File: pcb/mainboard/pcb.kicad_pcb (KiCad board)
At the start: 4 copper layers, 67.2 x 58.2 mm, 225 parts, among them J401 AudioJack3, J501 Conn_02x15_Odd_Even_MountingP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, J601 Conn_01x40_MountingPin, J801 USB_B_Mini, J901 U.FL Connector, SW101 SW_Push, SW201 SW_Push, U101 PCA9450BHN, U102 BQ27441-G1, U103 BQ24072RGT, U201 MIMX8MN6DVTJZAA, U302 MT53D512M16D1DS-046, U402 FSA2269UMX, U403 WM8978, U502 TPS65632, U702 W25Q128JVP, U802 USBLC6-2P6, U901 AP6330(BCM4330), Y101 32.768K, Y201 24MHz, Y901 26MHz

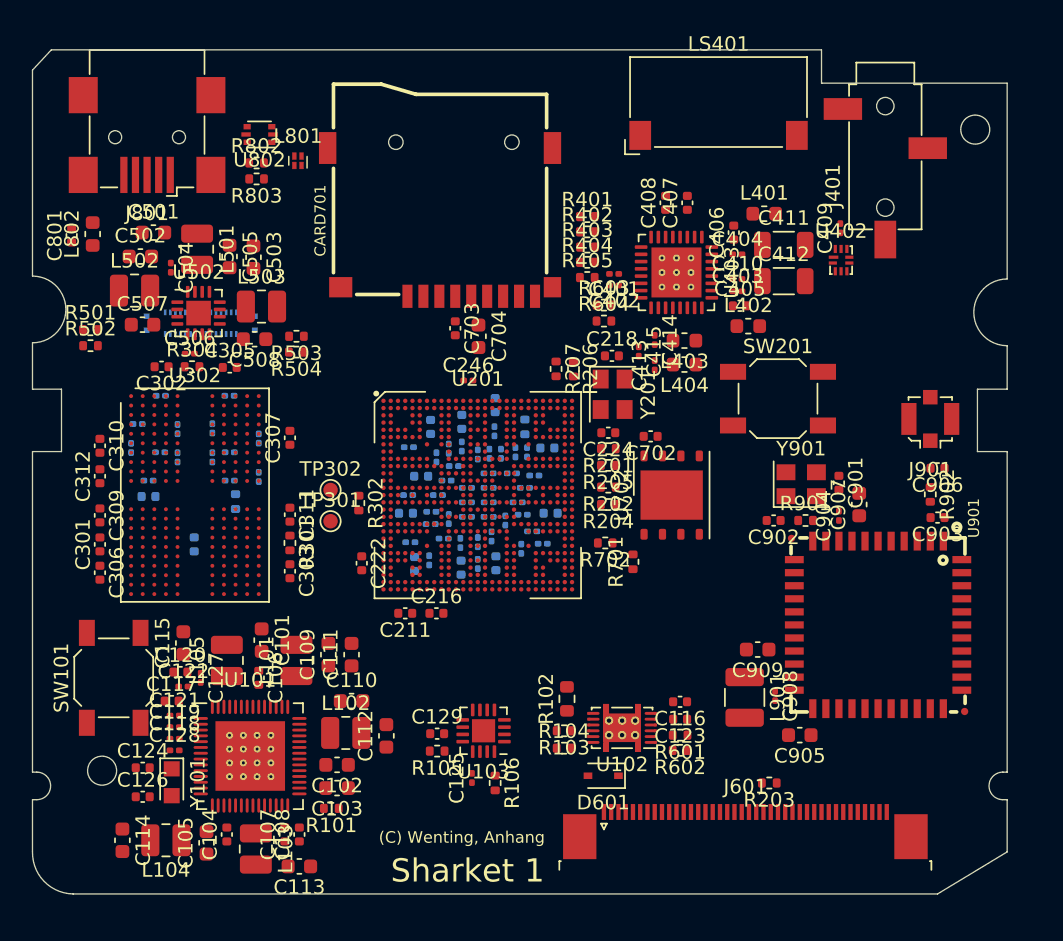
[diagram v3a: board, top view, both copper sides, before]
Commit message: Routing mainboard in progress, schematics fixes
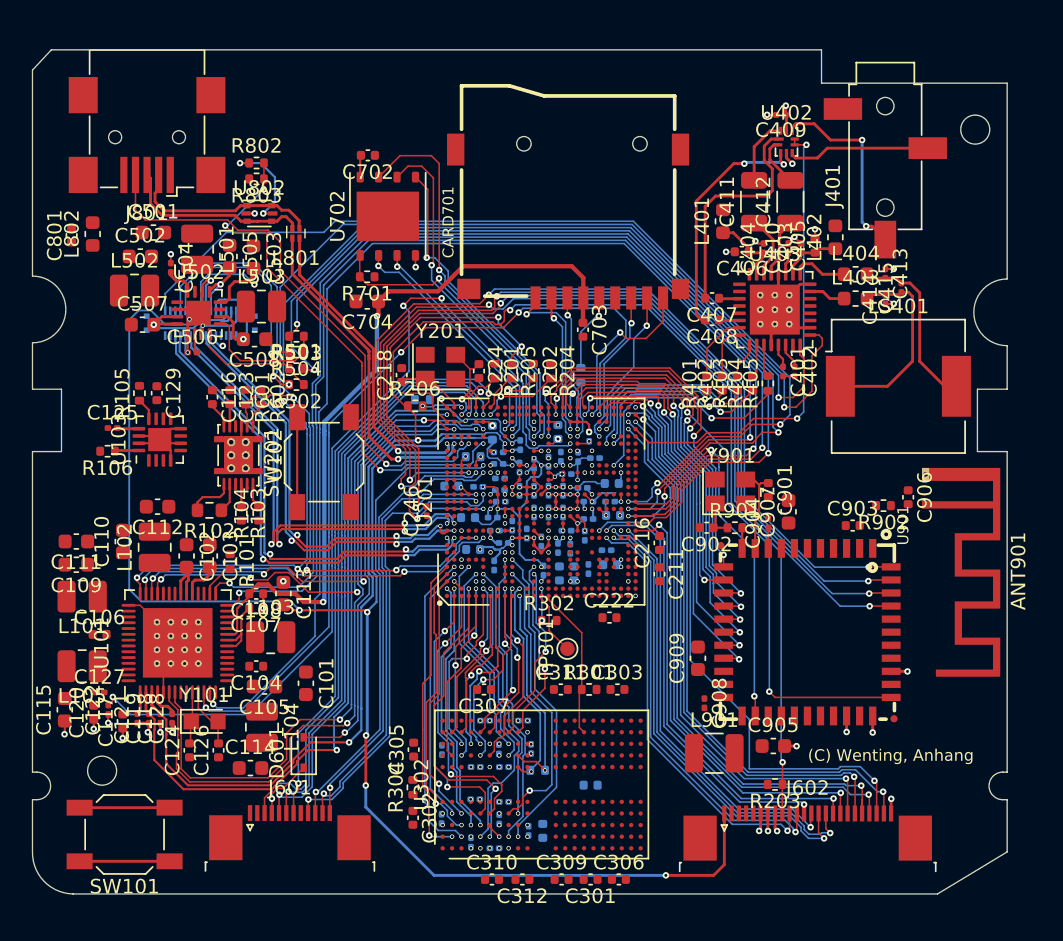
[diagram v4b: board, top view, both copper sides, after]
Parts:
- removed J901: U.FL Connector, Connector_Coaxial:U.FL_Molex_MCRF_73412-0110_Vertical
- removed R603, R604: 4.7K, Resistor_SMD:R_0402_1005Metric
- removed TP302: TestPoint, TestPoint:TestPoint_Pad_D1.0mm
- added ANT901: Conn_01x02, RF_Antenna:Texas_SWRA117D_2.4GHz_Right, F.Cu at (180.2, 100.1)
- added J602: Conn_01x24_MountingPin, Connector_FFC-FPC:TE_2-1734839-4_1x24-1MP_P0.5mm_Horizontal, F.Cu at (172.1, 122.7)
- J601: value Conn_01x40_MountingPin -> Conn_01x12_MountingPin; footprint Connector_FFC-FPC:TE_4-1734839-0_1x40-1MP_P0.5mm_Horizontal -> Connector_FFC-FPC:TE_1-1734839-2_1x12-1MP_P0.5mm_Horizontal
- LS401: footprint Buzzer_Beeper:Speaker_CUI_CMR-1206S-67 -> Buzzer_Beeper:Buzzer_CUI_CPT-9019S-SMT
- R207, R702: moved to B.Cu
- U302: footprint Package_BGA:BGA-200_10.0x14.5mm_Layout12x22_P0.80x0.65mm -> footprint:BGA-200_10.0x14.5mm_Layout12x22_P0.80x0.65mm_B0.3mm
- moved C306 41.6 mm to (159.0, 125.9), turned to 0 degrees
- moved C301 41.0 mm to (157.1, 125.9), turned to 180 degrees
- moved C309 40.5 mm to (155.1, 125.9), turned to 0 degrees
- moved C310 40.3 mm to (150.3, 125.9), turned to 0 degrees
- moved C312 40.3 mm to (152.4, 125.9), turned to 180 degrees
- moved C116 38.5 mm to (131.0, 92.7), turned to -90 degrees
- moved C123 38.2 mm to (132.2, 92.7), turned to -90 degrees
- moved R601 37.9 mm to (133.3, 92.7), turned to -90 degrees
- moved R602 37.8 mm to (134.3, 92.7), turned to -90 degrees
- moved C316 37.3 mm to (150.5, 123.8), turned to 0 degrees
- moved C314 36.9 mm to (148.8, 123.3), turned to 90 degrees
- moved C308 35.6 mm to (153.8, 122.5), turned to -90 degrees
- moved C325 35.6 mm to (152.8, 122.5), turned to -90 degrees
- moved C302 35.6 mm to (144.8, 121.7), turned to -90 degrees
- moved R106 35.2 mm to (123.8, 96.4), turned to 180 degrees
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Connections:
- C401 pad 2: Net-(C401-Pad2) -> GND
- C402 pad 2: Net-(C401-Pad2) -> GND
- C403 pad 2: Net-(C401-Pad2) -> GND
- C404 pad 2: Net-(C401-Pad2) -> GND
- J601 pad 2: GND -> +1V8
- L801 pad 1: USB_DP -> /usb/USB_PORT_DP
- L801 pad 2: USB_DN -> /usb/USB_PORT_DN
- L801 pad 3: /usb/USB_PORT_DN -> USB_DN
- L801 pad 4: /usb/USB_PORT_DP -> USB_DP
- R205 pad 1: Net-(R205-Pad1) -> RTC_1P8
- R206 pad 1: Net-(R205-Pad1) -> RTC_1P8
- U201 pad AB22: TASKSEL -> unconnected-(U201-PadAB22)
- U201 pad AF11: LCD_RST -> unconnected-(U201-PadAF11)
- U201 pad AF14: unconnected-(U201-PadAF14) -> LCD_RST
- U201 pad AG24: unconnected-(U201-PadAG24) -> TASKSEL
- U201 pad E10: I2C3_SCL -> unconnected-(U201-PadE10)
- U201 pad F10: I2C3_SDA -> unconnected-(U201-PadF10)
- U201 pad N2: Net-(TP302-Pad1) -> unconnected-(U201-PadN2)
- U201 pad U26: BT_WAKE -> unconnected-(U201-PadU26)
- U201 pad W26: WL_WAKE_AP -> unconnected-(U201-PadW26)
- U201 pad W27: BT_HOST_WAKE -> WL_WAKE_AP
- U403 pad 16: I2C3_SCL -> I2C1_SCL
- U403 pad 17: I2C3_SDA -> I2C1_SDA
- U901 pad 6: BT_WAKE -> unconnected-(U901-Pad6)
- U901 pad 7: BT_HOST_WAKE -> unconnected-(U901-Pad7)
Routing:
- net +3V3: track 0.00 -> 114.2 mm, vias 0 -> 6
- net GND: track 0.00 -> 103.0 mm, vias 0 -> 112
- net I2C1_SDA: track 0.00 -> 101.2 mm, vias 0 -> 6
- net I2C1_SCL: track 0.00 -> 97.4 mm, vias 0 -> 6
- net PMIC_INT: track 0.00 -> 84.0 mm, vias 0 -> 4
- net SD2_VSEL: track 0.00 -> 80.1 mm, vias 0 -> 2
- net WDOG_B: track 0.00 -> 78.1 mm, vias 0 -> 2
- net RTC_1P8: track 0.00 -> 71.0 mm, vias 0 -> 5
- net UART1_TXD: track 0.00 -> 67.7 mm, vias 0 -> 4
- net LCD_RST: track 0.00 -> 67.3 mm, vias 0 -> 3
- net UART1_RXD: track 0.00 -> 65.9 mm, vias 0 -> 4
- net UART1_CTS: track 0.00 -> 65.9 mm, vias 0 -> 4
- net ONOFF: track 0.00 -> 65.7 mm, vias 0 -> 2
- net UART1_RTS: track 0.00 -> 64.5 mm, vias 0 -> 4
- net AVDD_EN: track 0.00 -> 63.1 mm, vias 0 -> 4
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- added copper zone on In2.Cu, net GND
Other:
- board text removed: "Sharket 1"

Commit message: Update layout
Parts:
- moved R203 36.3 mm to (145.0, 92.8)
- moved C113 3.61 mm to (137.9, 109.2), turned to 90 degrees
- moved C246 3.28 mm to (145.7, 103.8)
- moved R302 1.88 mm to (156.1, 107.8)
- moved C114 1.59 mm to (132.2, 117.5), turned to 90 degrees
- moved C126 0.97 mm to (130.5, 117.0)
- moved R502 0.90 mm to (135.9, 91.8)
- moved R206 0.55 mm to (145.0, 93.8)
- moved C127 0.52 mm to (122.8, 112.7)
- moved L101 0.50 mm to (122.0, 106.9)
- moved L105 0.41 mm to (122.0, 110.8)
- moved C111 0.35 mm to (121.6, 103.0)
- moved C109 0.35 mm to (121.6, 104.5)
- moved C106 0.14 mm to (123.2, 108.9)
- moved C313 0.08 mm to (150.8, 117.0)
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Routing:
- net +BATT: track 14.2 -> 189.5 mm, vias 0 -> 9
- net GND: track 103.0 -> 219.6 mm, vias 112 -> 256
- net BATP: track 3.94 -> 75.9 mm, vias 0 -> 5
- net +3V3: track 114.2 -> 172.7 mm, vias 6 -> 7
- net +1V8A: track 20.2 -> 74.6 mm, vias 7 -> 8
- net VDD_SOC: track 11.1 -> 58.9 mm, vias 16 -> 24
- net +1V2: track 1.88 -> 44.6 mm, vias 1 -> 3
- net +1V8: track 20.9 -> 62.8 mm, vias 18 -> 34
- net +1V1: track 10.8 -> 47.1 mm, vias 22 -> 55
- net VDD_ARM: track 9.89 -> 38.1 mm, vias 11 -> 16
- net Net-(J801-Pad1): track 6.93 -> 23.3 mm
- net VBUS: track 1.52 -> 16.3 mm
- net Net-(R206-Pad2): track 9.01 -> 19.2 mm, vias 2 -> 3
- net POR_B: track 29.4 -> 39.6 mm, vias 2 -> 4
- net SDRAM_CA4: track 12.3 -> 21.1 mm
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- added copper zone on F.Cu, net +1V1
- added copper zone on In1.Cu, net +1V1
- added copper zone on F.Cu, net +1V8
- added copper zone on In1.Cu, net +1V8
- added copper zone on F.Cu, net +3V3
- added copper zone on F.Cu, net +BATT
- added copper zone on F.Cu, net Net-(C905-Pad1)
- added copper zone on F.Cu, net Net-(L101-Pad1)
- added copper zone on F.Cu, net Net-(L102-Pad1)
- added copper zone on F.Cu, net Net-(L103-Pad1)
- added copper zone on F.Cu, net Net-(L104-Pad1)
- added copper zone on F.Cu, net Net-(L105-Pad1)
- added copper zone on F.Cu, net Net-(L501-Pad2)
- added copper zone on F.Cu, net Net-(L502-Pad2)
- added copper zone on F.Cu, net Net-(L503-Pad1)
- added copper zone on F.Cu, net Net-(L901-Pad1)
- added copper zone on F.Cu, net VDD_ARM
- added copper zone on In1.Cu, net VDD_ARM
- added copper zone on F.Cu, net VDD_SOC
- added copper zone on In1.Cu, net VDD_SOC

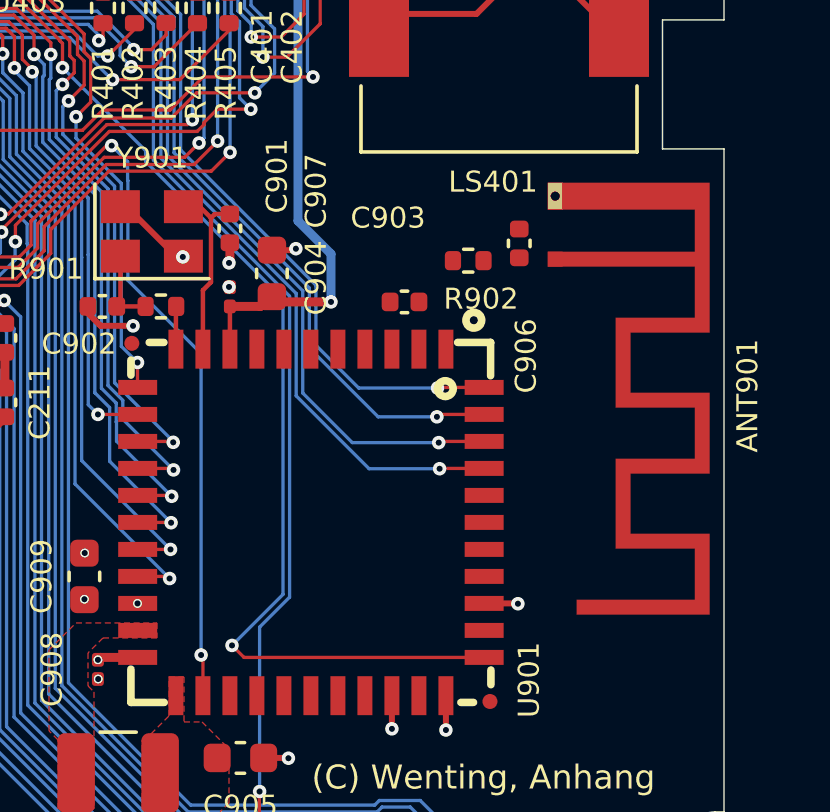
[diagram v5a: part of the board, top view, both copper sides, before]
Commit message: Minor - Layout wifi antenna
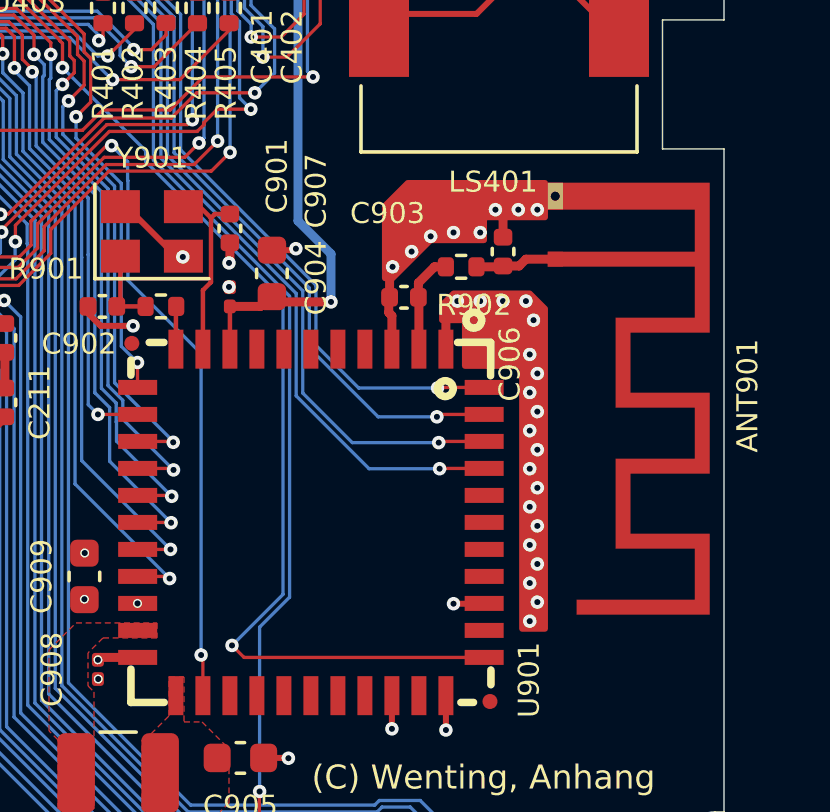
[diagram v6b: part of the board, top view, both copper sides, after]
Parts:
- moved C906 0.60 mm to (178.4, 99.8)
- moved R902 0.31 mm to (177.0, 100.3)
- moved C903 0.15 mm to (175.1, 101.3)
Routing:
- net GND: track 219.6 -> 225.7 mm, vias 256 -> 284
- net Net-(C903-Pad2): track 0.00 -> 3.35 mm
- net Net-(C906-Pad2): track 0.00 -> 2.73 mm

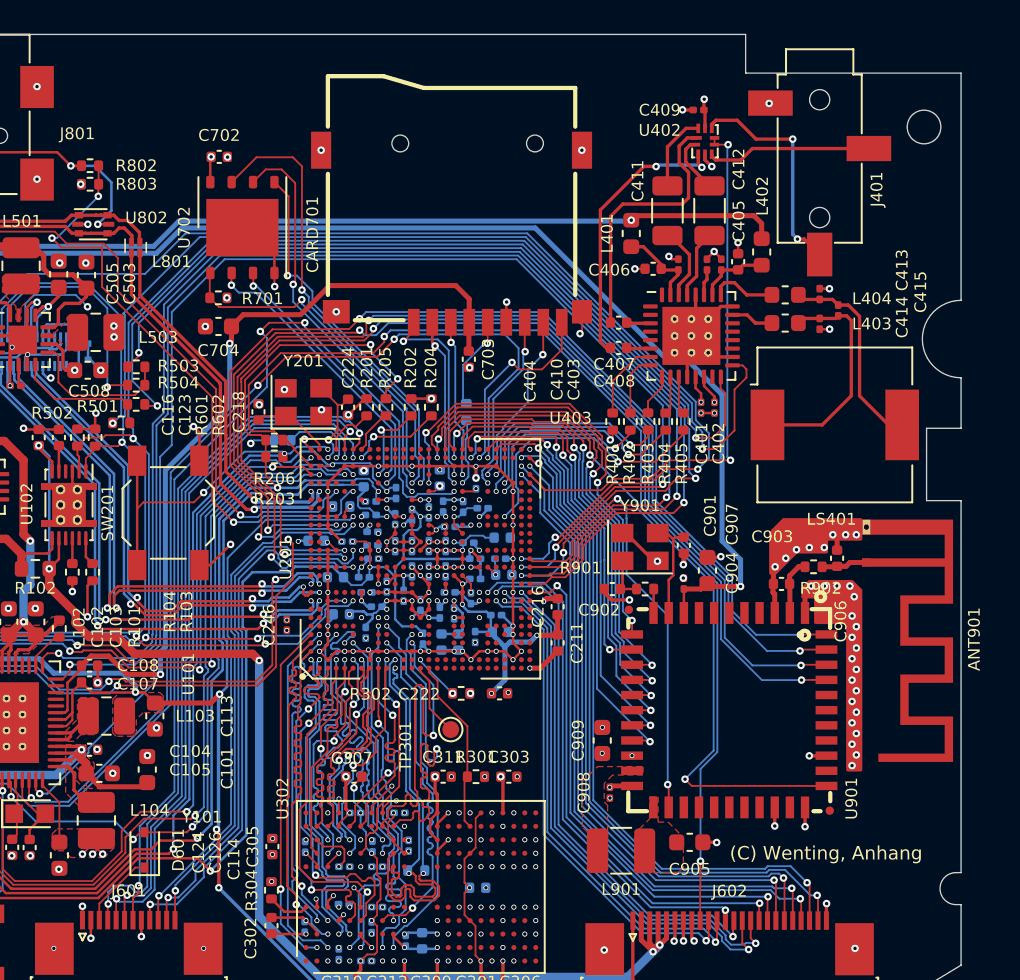
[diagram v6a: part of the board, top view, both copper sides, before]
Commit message: Mainboard design bug fixes
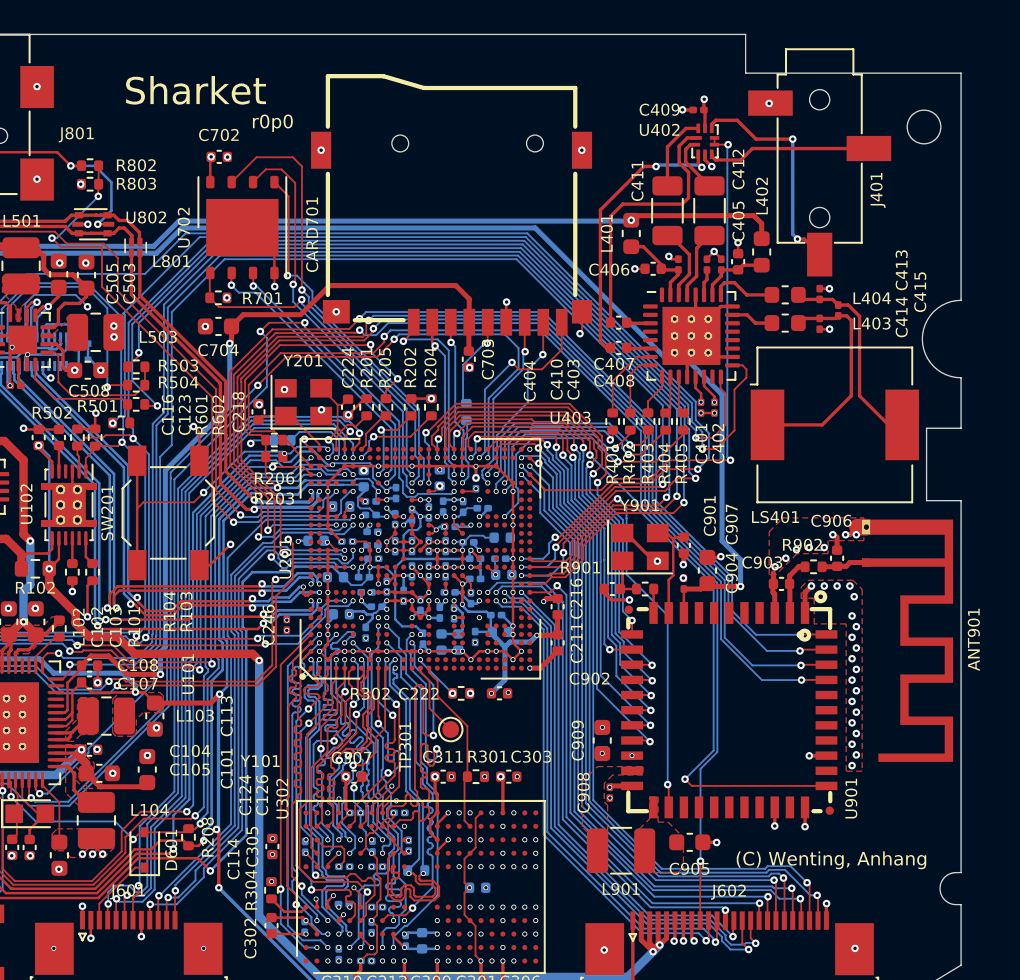
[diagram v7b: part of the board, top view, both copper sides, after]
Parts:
- added R208: 100K, Resistor_SMD:R_0402_1005Metric, F.Cu at (139.9, 116.4)
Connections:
- U103 pad 5: unconnected-(U103-Pad5) -> +BATT
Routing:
- net RTC_1P8: track 71.1 -> 71.6 mm
- net VDD_ARM: vias 16 -> 17
- added copper zone on F.Cu, net GND
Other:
- board text added: "Sharket"
- board text added: "r0p0"
